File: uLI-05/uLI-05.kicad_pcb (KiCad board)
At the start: 2 copper layers, 58 x 39.5 mm, 49 parts, among them J2 USB_B, J3 RJ25, J4 RJ25, J5 PROG, Q1 IRF7306, U1 LM78M05_TO252, U2 PC817, U3 PC817, U4 PIC18F14K50-EP, U5 ADM2483xRW, U6 USBLC6-2SC6, Y1 12MHz

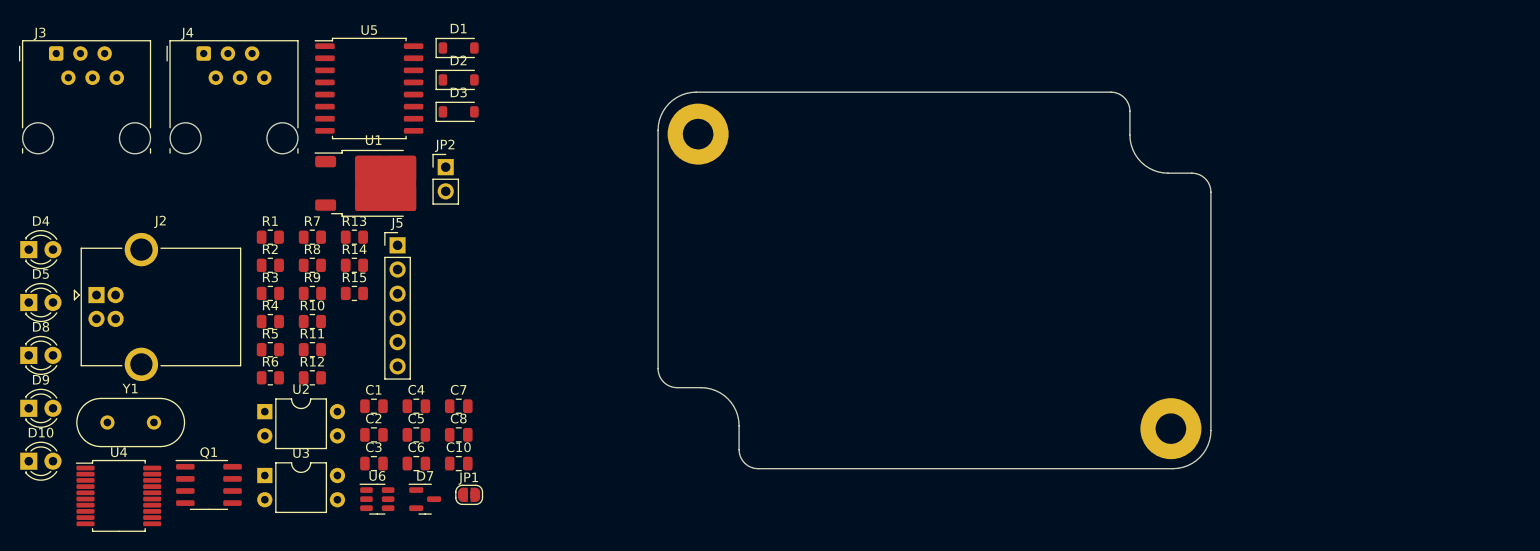
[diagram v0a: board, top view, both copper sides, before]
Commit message: pcb: place connectors & LEDs.
Place on same positions as in uLI-4.
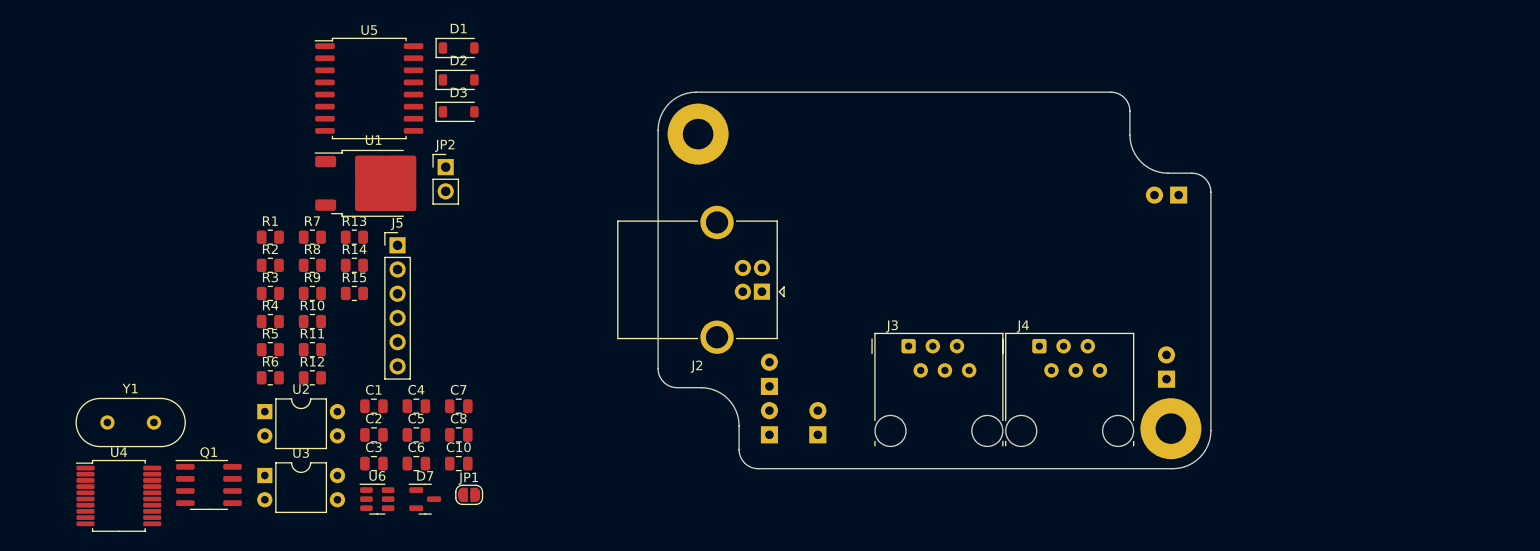
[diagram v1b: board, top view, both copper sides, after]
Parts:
- D10, D4, D5, D8, D9: moved to B.Cu
- Y1: footprint Crystal:Crystal_HC49-U_Vertical -> Crystal:Crystal_HC49-4H_Vertical
- moved D4 120.8 mm to (181.0, 93.2), turned to 180 degrees
- moved D5 119.6 mm to (179.7, 112.5), turned to 90 degrees
- moved J3 94.5 mm to (152.7, 109.1)
- moved J4 92.9 mm to (166.4, 109.1)
- moved D10 82.8 mm to (143.1, 118.4), turned to 90 degrees
- moved D8 77.8 mm to (138.1, 113.3), turned to 90 degrees
- moved D9 77.8 mm to (138.1, 118.4), turned to 90 degrees
- moved J2 69.8 mm to (137.3, 103.4), turned to 180 degrees

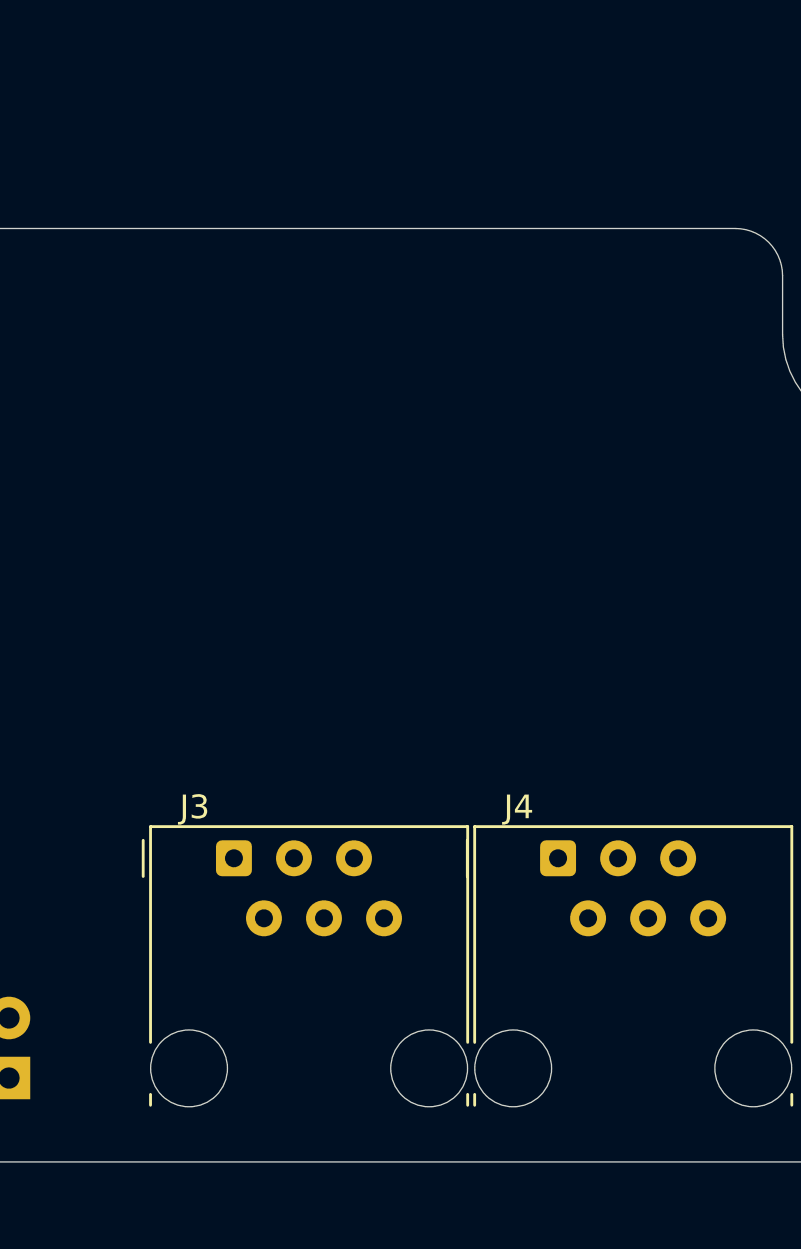
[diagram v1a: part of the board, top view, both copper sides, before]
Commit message: Add STL1550 power connector.
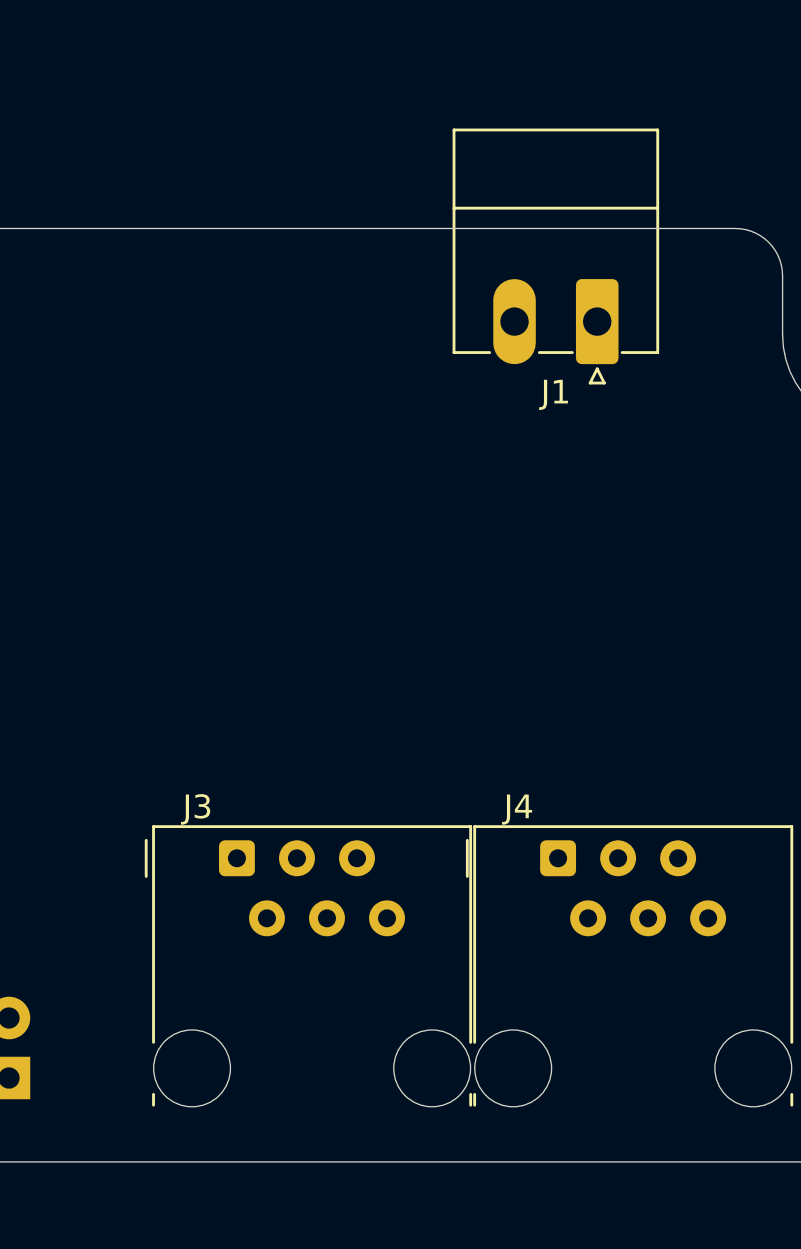
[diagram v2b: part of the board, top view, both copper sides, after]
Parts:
- added J1: STL1550, Connector_Phoenix_MC:PhoenixContact_MC_1,5_2-G-3.5_1x02_P3.50mm_Horizontal, F.Cu at (168.0, 86.4)
- moved J3 0.13 mm to (152.8, 109.1)
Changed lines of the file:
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@@
     (property "ki_keywords" "connector USB")
     (attr through_hole)
-    (fp_text reference "J2" (at 6.76 -7.77) (layer "F.SilkS")
-        (effects (font (size 1 1) (thickness 0.15)))
-    )
-    (fp_text value "USB_B" (at 6.76 10.27) (layer "F.Fab")
-        (effects (font (size 1 1) (thickness 0.15)))
-    )
-    (fp_text user "${REFERENCE}" (at 6.76 1.25) (layer "F.Fab")
+    (fp_text reference "J2" (at 6.76 -7.77 180) (layer "F.SilkS")
+        (effects (font (size 1 1) (thickness 0.15)))
+    )
+    (fp_text value "USB_B" (at 6.76 10.27 180) (layer "F.Fab")
+        (effects (font (size 1 1) (thickness 0.15)))
+    )
+    (fp_text user "${REFERENCE}" (at 6.76 1.25 180) (layer "F.Fab")
         (effects (font (size 1 1) (thickness 0.15)))
     )
@@
       (net 20 "D+{slash}PGD") (pinfunction "I/O1") (pintype "passive"))
     (model "${KICAD6_3DMODEL_DIR}/Package_TO_SOT_SMD.3dshapes/SOT-23-6.wrl"
+      (offset (xyz 0 0 0))
+      (scale (xyz 1 1 1))
+      (rotate (xyz 0 0 0))
+    )
+  )
+  (footprint "Connector_Phoenix_MC:PhoenixContact_MC_1,5_2-G-3.5_1x02_P3.50mm_Horizontal" (layer "F.Cu")
+    (at 168.032 86.378 180)
+    (descr "Generic Phoenix Contact connector footprint for: MC_1,5/2-G-3.5; number of pins: 02; pin pitch: 3.50mm; Angled || order number: 1844210 8A 160V")
+    (tags "phoenix_contact connector MC_01x02_G_3.5mm")
+    (property "Sheetfile" "uLI-05.kicad_sch")
+    (property "Sheetname" "")
+    (property "ki_description" "Generic connector, single row, 01x02, script generated (kicad-library-utils/schlib/autogen/connector/)")
+    (property "ki_keywords" "connector")
+    (attr through_hole)
+    (fp_text reference "J1" (at 1.75 -3) (layer "F.SilkS")
+        (effects (font (size 1 1) (thickness 0.15)))
+    )
+    (fp_text value "STL1550" (at 1.75 9.2) (layer "F.Fab")
+        (effects (font (size 1 1) (thickness 0.15)))
+    )
+    (fp_text user "${REFERENCE}" (at 1.75 -0.5) (layer "F.Fab")
+        (effects (font (size 1 1) (thickness 0.15)))
+    )
+    (fp_line (start -2.56 -1.31) (end -2.56 8.11)
+      (stroke (width 0.12) (type solid)) (layer "F.SilkS"))
+    (fp_line (start -2.56 -1.31) (end -1.05 -1.31)
+      (stroke (width 0.12) (type solid)) (layer "F.SilkS"))
+    (fp_line (start -2.56 4.8) (end 6.06 4.8)
+      (stroke (width 0.12) (type solid)) (layer "F.SilkS"))
+    (fp_line (start -2.56 8.11) (end 6.06 8.11)
+      (stroke (width 0.12) (type solid)) (layer "F.SilkS"))
+    (fp_line (start -0.3 -2.6) (end 0.3 -2.6)
+      (stroke (width 0.12) (type solid)) (layer "F.SilkS"))
+    (fp_line (start 0 -2) (end -0.3 -2.6)
+      (stroke (width 0.12) (type solid)) (layer "F.SilkS"))
+    (fp_line (start 0.3 -2.6) (end 0 -2)
+      (stroke (width 0.12) (type solid)) (layer "F.SilkS"))
+    (fp_line (start 1.05 -1.31) (end 2.45 -1.31)
+      (stroke (width 0.12) (type solid)) (layer "F.SilkS"))
+    (fp_line (start 6.06 -1.31) (end 4.55 -1.31)
+      (stroke (width 0.12) (type solid)) (layer "F.SilkS"))
+    (fp_line (start 6.06 8.11) (end 6.06 -1.31)
+      (stroke (width 0.12) (type solid)) (layer "F.SilkS"))
+    (fp_line (start -3.06 -2.3) (end -3.06 8.5)
+      (stroke (width 0.05) (type solid)) (layer "F.CrtYd"))
+    (fp_line (start -3.06 8.5) (end 6.45 8.5)
+      (stroke (width 0.05) (type solid)) (layer "F.CrtYd"))
+    (fp_line (start 6.45 -2.3) (end -3.06 -2.3)
+      (stroke (width 0.05) (type solid)) (layer "F.CrtYd"))
+    (fp_line (start 6.45 8.5) (end 6.45 -2.3)
+      (stroke (width 0.05) (type solid)) (layer "F.CrtYd"))
+    (fp_line (start -2.45 -1.2) (end -2.45 8)
+      (stroke (width 0.1) (type solid)) (layer "F.Fab"))
+    (fp_line (start -2.45 8) (end 5.95 8)
+      (stroke (width 0.1) (type solid)) (layer "F.Fab"))
+    (fp_line (start 0 0) (end -0.8 -1.2)
+      (stroke (width 0.1) (type solid)) (layer "F.Fab"))
+    (fp_line (start 0.8 -1.2) (end 0 0)
+      (stroke (width 0.1) (type solid)) (layer "F.Fab"))
+    (fp_line (start 5.95 -1.2) (end -2.45 -1.2)
+      (stroke (width 0.1) (type solid)) (layer "F.Fab"))
+    (fp_line (start 5.95 8) (end 5.95 -1.2)
+      (stroke (width 0.1) (type solid)) (layer "F.Fab"))
+    (pad "1" thru_hole roundrect (at 0 0 180) (size 1.8 3.6) (drill 1.2) (layers "*.Cu" "*.Mask") (roundrect_rratio 0.138889)
+      (net 11 "Net-(D2-A)") (pinfunction "Pin_1") (pintype "passive"))
+    (pad "2" thru_hole oval (at 3.5 0 180) (size 1.8 3.6) (drill 1.2) (layers "*.Cu" "*.Mask")
+      (net 7 "GNDA") (pinfunction "Pin_2") (pintype "passive"))
+    (model "${KICAD6_3DMODEL_DIR}/Connector_Phoenix_MC.3dshapes/PhoenixContact_MC_1,5_2-G-3.5_1x02_P3.50mm_Horizontal.wrl"
       (offset (xyz 0 0 0))
       (scale (xyz 1 1 1))
@@
   )
   (footprint "Connector_RJ:RJ12_Amphenol_54601-x06_Horizontal" (layer "F.Cu")
-    (at 152.66 109.088)
+    (at 152.787 109.088)
     (descr "RJ12 6P6C horizontal socket, plastic body, tab down, https://cdn.amphenol-icc.com/media/wysiwyg/files/drawing/c-bmj-0082.pdf")
     (tags "RJ12 connector")

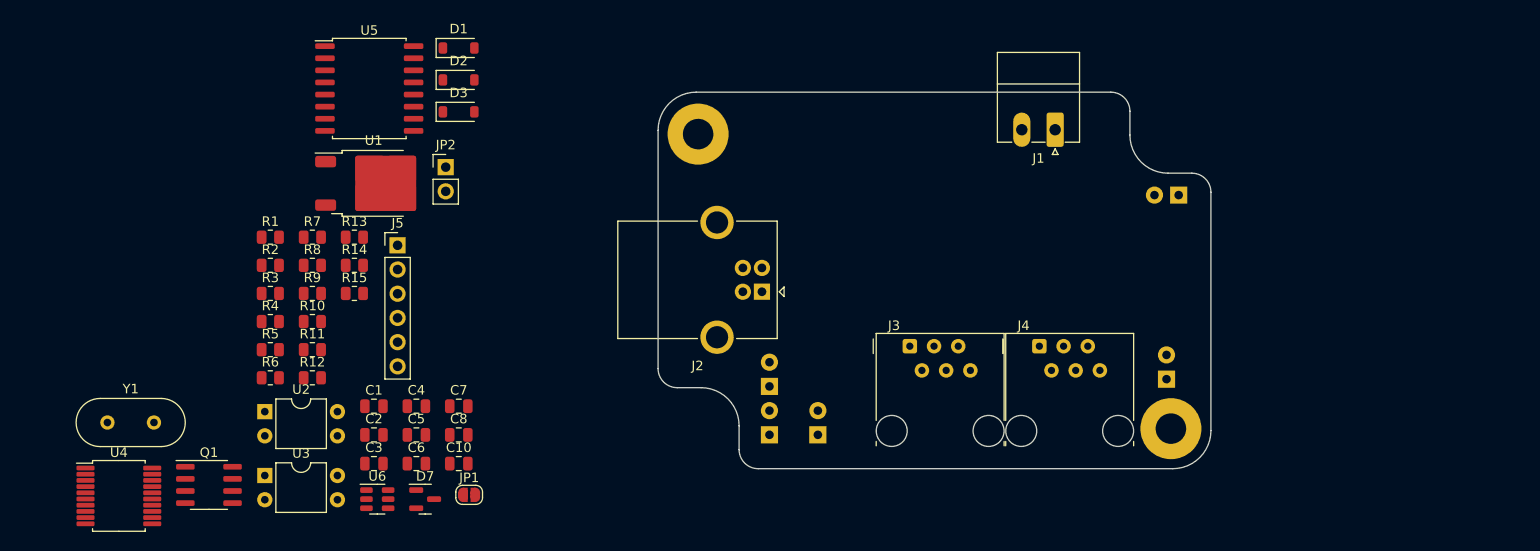
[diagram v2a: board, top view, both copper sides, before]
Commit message: pcb: wire USB part.
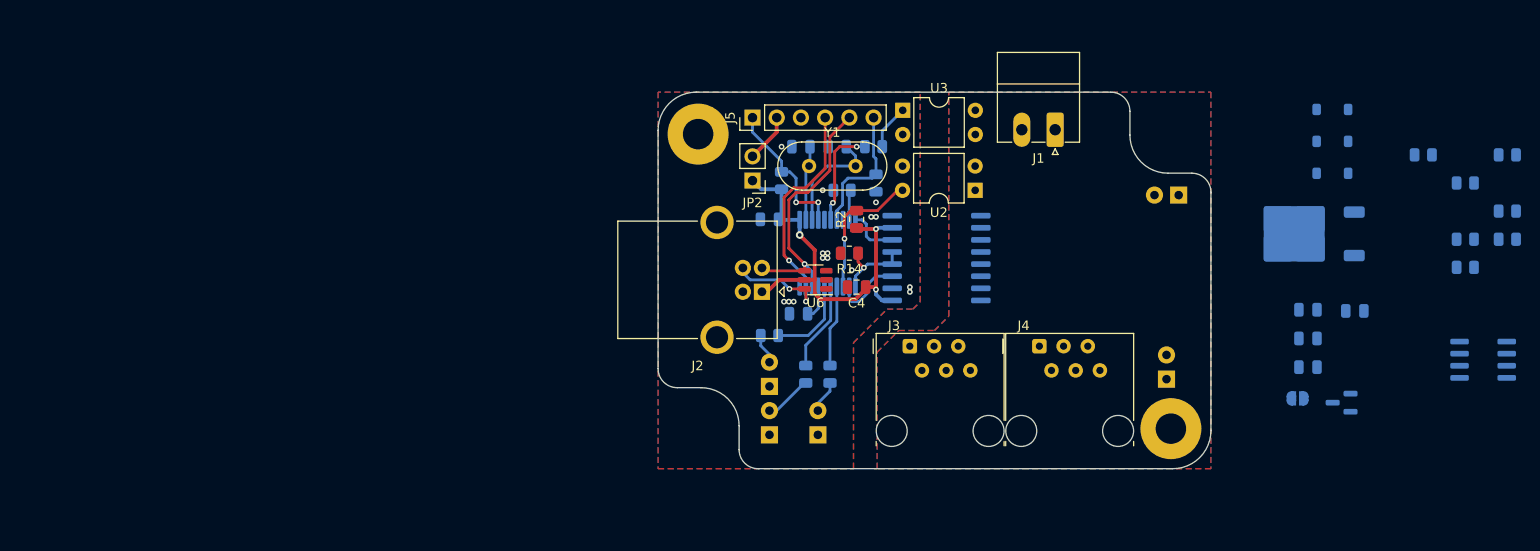
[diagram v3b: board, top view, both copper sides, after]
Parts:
- added R16: 10k, Resistor_SMD:R_0805_2012Metric, B.Cu at (145.7, 92.7)
- C1, C10, C2, C3, C5, C6, C7, C8, D1, D2, D3, D7, JP1, Q1, R1, R10, R11, R12, R13, R15, R3, R4, R5, R6, R7, R8, R9, U1, U4, U5: moved to B.Cu
- moved Q1 134.3 mm to (212.9, 110.5), turned to 180 degrees
- moved R1 130.1 mm to (215.5, 89.0), turned to 180 degrees
- moved R3 130.1 mm to (215.5, 94.9), turned to 180 degrees
- moved R4 130.1 mm to (215.5, 97.9), turned to 180 degrees
- moved R10 121.3 mm to (211.1, 97.9), turned to 180 degrees
- moved R11 121.3 mm to (211.1, 100.8), turned to 180 degrees
- moved R8 121.3 mm to (211.1, 92.0), turned to 180 degrees
- moved R13 112.5 mm to (206.7, 89.0), turned to 180 degrees
- moved C6 99.7 mm to (199.5, 105.4), turned to 180 degrees
- moved U1 98.0 mm to (194.4, 97.3), turned to 180 degrees
- moved D7 96.7 mm to (198.1, 115.0), turned to 180 degrees
- moved D1 91.9 mm to (197.1, 84.2), turned to 180 degrees
- moved D2 91.9 mm to (197.1, 87.6), turned to 180 degrees
- moved D3 91.9 mm to (197.1, 91.0), turned to 180 degrees
- moved C10 89.7 mm to (194.6, 111.3), turned to 180 degrees
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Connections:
- D10 pad 1: GNDA -> GND
- D8 pad 1: GNDA -> GND
- D9 pad 1: GNDA -> GND
- U4 pad 15: LED_GR1 -> LED_GR2
- U4 pad 16: LED_GR2 -> LED_GR1
- U6 pad 1: D+/PGD -> unconnected-(U6-I/O1-Pad1)
- U6 pad 3: D-/PGC -> unconnected-(U6-I/O2-Pad3)
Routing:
- net VCC: track 0.00 -> 43.7 mm, vias 0 -> 3
- net D+/PGD: track 0.00 -> 31.8 mm, vias 0 -> 3
- net D-/PGC: track 0.00 -> 27.4 mm, vias 0 -> 1
- net MCLR: track 0.00 -> 15.5 mm, vias 0 -> 2
- net SENSE: track 0.00 -> 14.6 mm, vias 0 -> 1
- net PGM: track 0.00 -> 14.0 mm
- net Net-(U4-RA4/IOCA3/AN3/OSC2/CLKOUT): track 0.00 -> 11.8 mm
- net Net-(U4-SRQ/C12OUT/P1B/RC4): track 0.00 -> 10.7 mm, vias 0 -> 2
- net LED_GR2: track 0.00 -> 9.37 mm
- net LED_GR1: track 0.00 -> 8.99 mm
- net LED_YEL: track 0.00 -> 8.59 mm
- net /DE: track 0.00 -> 8.52 mm, vias 0 -> 1
- net Net-(U4-RA5/IOCA5/OSC1/CLKIN): track 0.00 -> 7.85 mm
- net /RX: track 0.00 -> 7.56 mm
- net /TX: track 0.00 -> 5.47 mm
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- added copper zone on B.Cu, net GND
- added copper zone on F.Cu, net GND
- added copper zone on B.Cu, net GNDA
- added copper zone on F.Cu, net GNDA
